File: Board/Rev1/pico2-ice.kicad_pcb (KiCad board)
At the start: 4 copper layers, 27.9 x 63.5 mm, 122 parts, among them J1 USB_C_Receptacle_USB2.0, J2 Conn_02x20_Odd_Even, J3 Conn_02x20_Odd_Even, J5 BM03B-SRSS-TB, J6 Conn_01x22_MountingPin, SW1 CS1213AGF260, SW2 CS1213AGF260, U1 NCP115AMX120TCG, U2 W25Q32JVSSIQ, U3 RP2350_80QFN, U4 TL431DBZ, U5 APS6404L-3SQN-SN, U6 ICE40UP5K-SG48ITR, U8 W25Q32JVSSIQ, U9 NCP115AMX330TCG, Y1 ABM8-272-T3

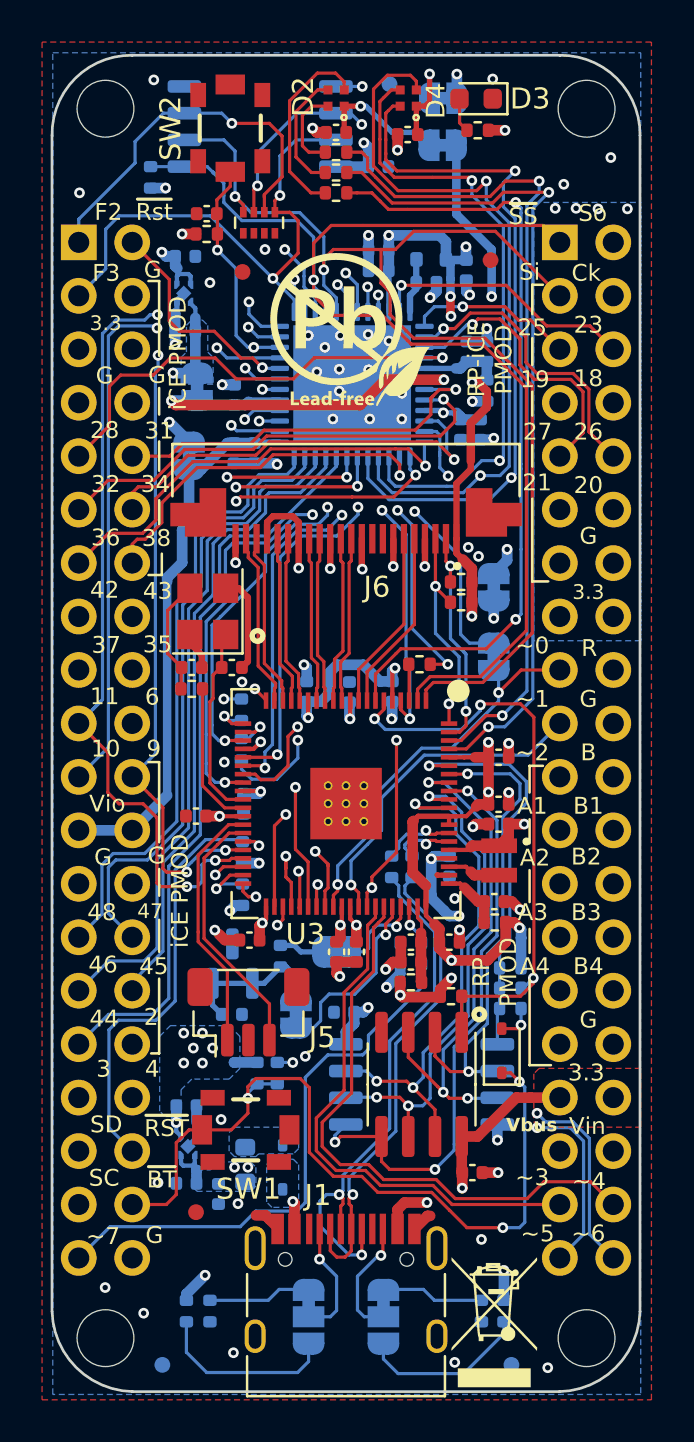
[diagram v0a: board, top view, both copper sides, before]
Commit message: Bugfixes for silkscreen PMOD, added DONE, unconnected RP22 pins, layout not yet complete
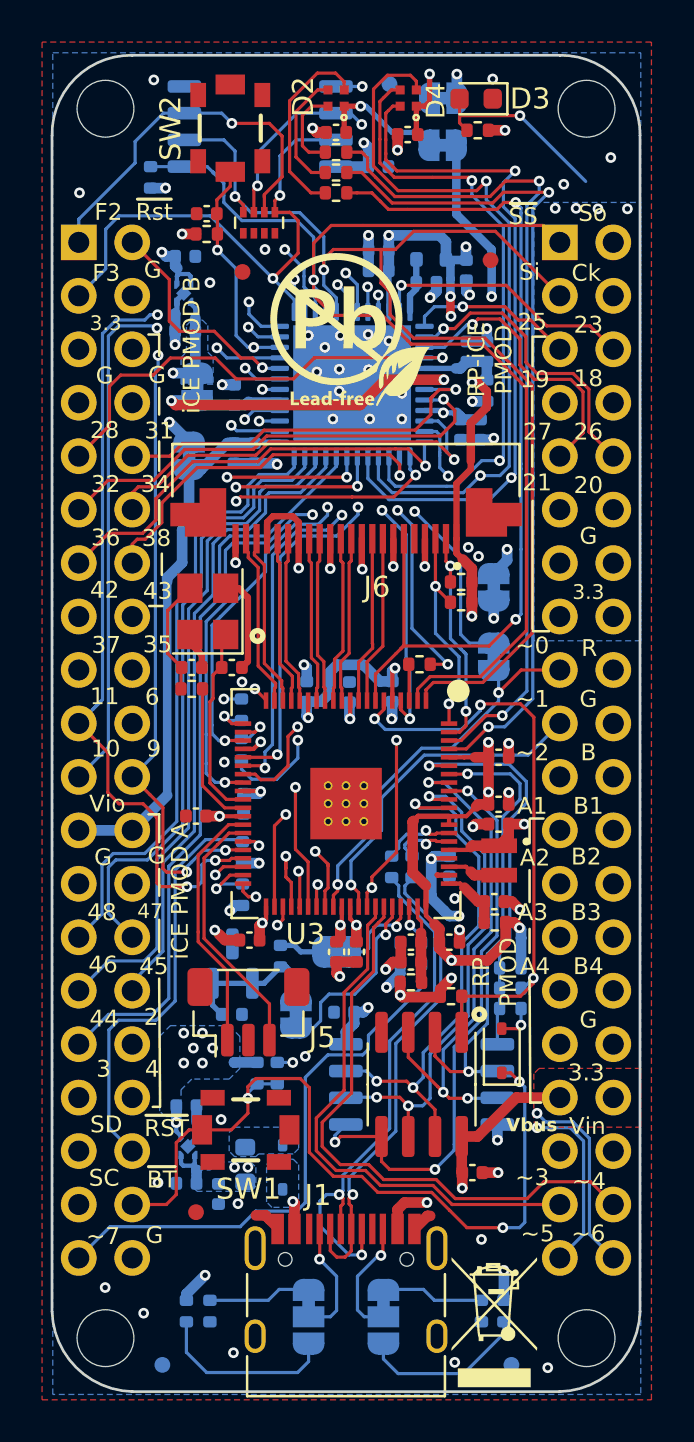
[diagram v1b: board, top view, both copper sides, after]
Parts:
- J6: value Conn_01x22_MountingPin -> FH12A-22S-0.5SH(55)
- R30, R31: value 0 -> SHORT
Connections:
- D3 pad 2: /ICE_DONE -> /ICE_DONE|ADC0
- J6 pad 5: /GPIO10 -> /LED_R
- J6 pad 6: /GPIO11 -> /LED_B
- J6 pad 8: unconnected-(J6-Pin_8-Pad8) -> /GPIO10
- J6 pad 9: unconnected-(J6-Pin_9-Pad9) -> /GPIO11
- R14 pad 1: /ICE_DONE -> /ICE_DONE|ADC0
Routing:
- net /ICE_DONE|ADC0: track 18.8 -> 27.7 mm, vias 2 -> 3
- net /LED_B: track 37.5 -> 42.8 mm
- net /ICE_DONE: track 1.65 -> 0.00 mm
- net /GPIO10: track 8.62 -> 8.00 mm
- net /GPIO11: track 8.58 -> 7.97 mm
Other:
- board text added: "iCE PMOD A"
- board text added: "iCE PMOD B"
- board text removed: "iCE PMOD"

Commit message: PCB file updated
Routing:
- net /ICE_DONE|ADC0: track 27.7 -> 51.9 mm
- net /LED_R: track 39.8 -> 50.1 mm, vias 2 -> 3
- net /ICE_27: track 37.0 -> 38.8 mm
- net /LED_B: track 42.8 -> 44.1 mm
- net +3V3: track 82.6 -> 83.4 mm

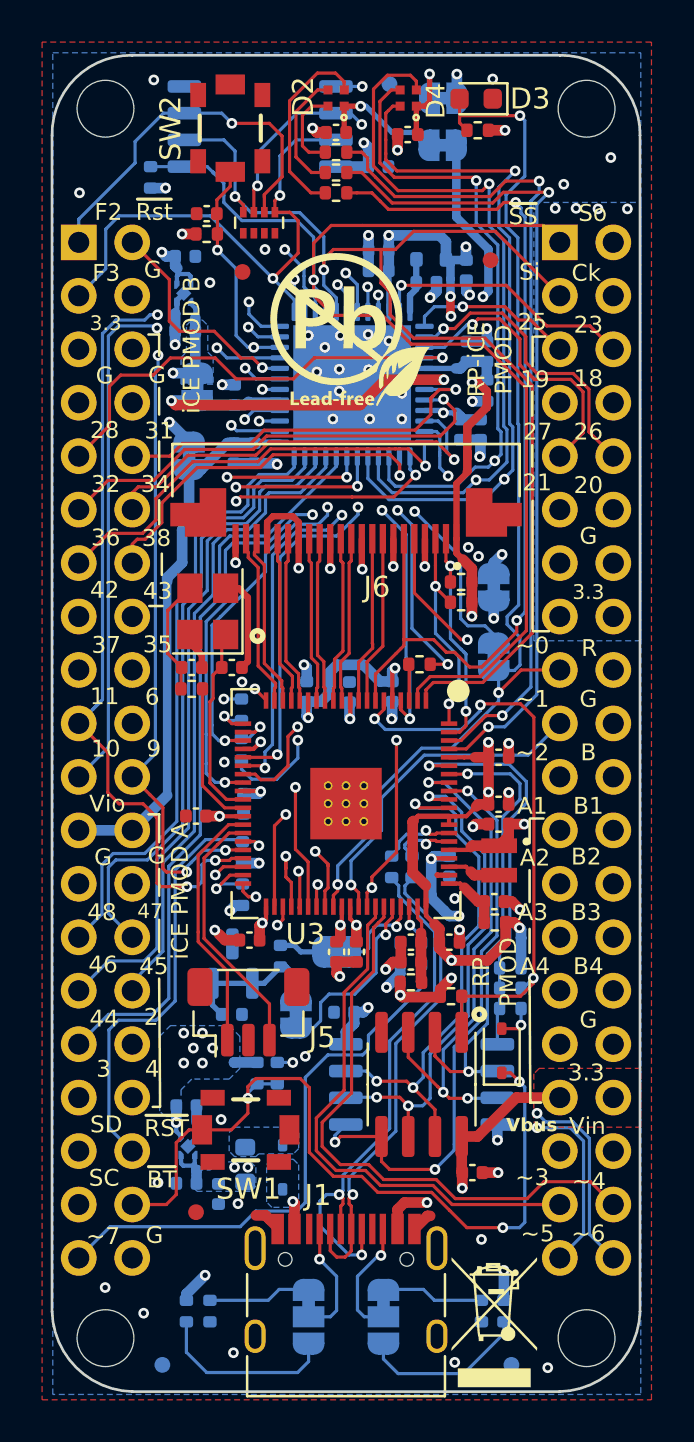
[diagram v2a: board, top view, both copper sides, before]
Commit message: Added voltage monitor
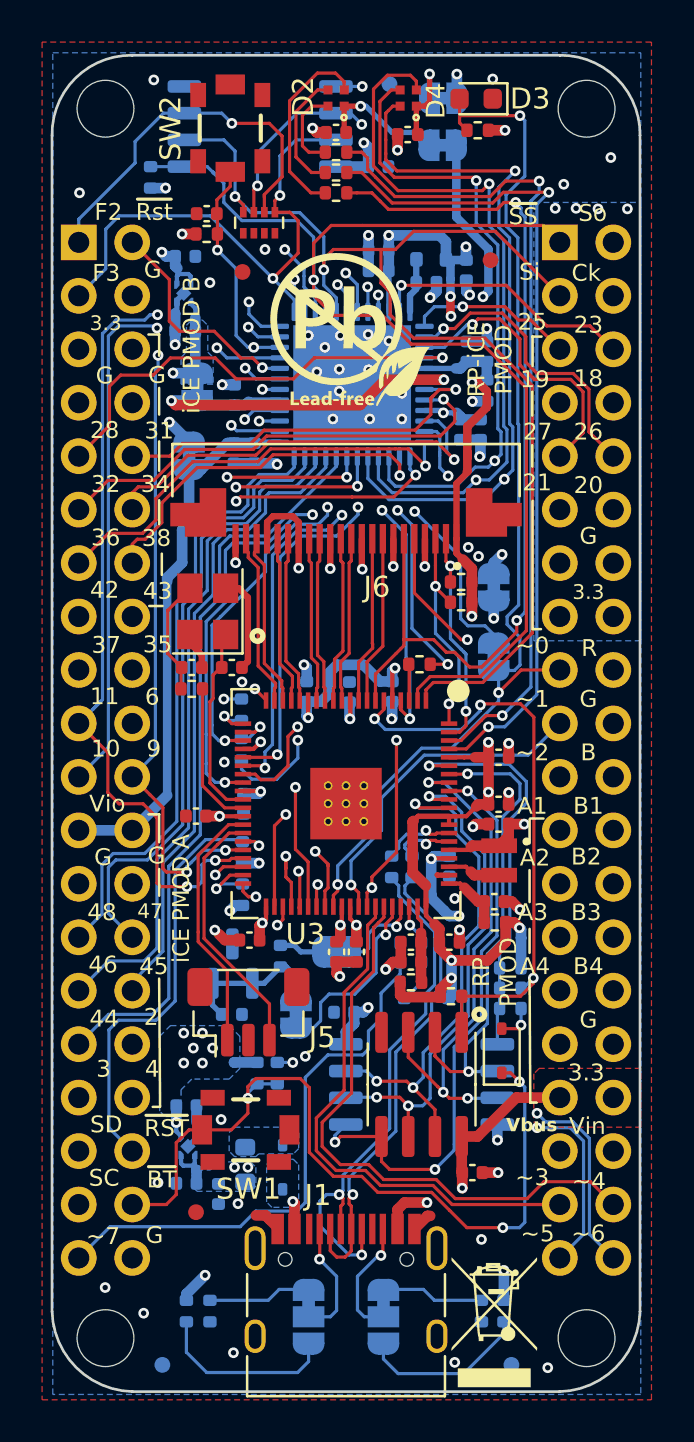
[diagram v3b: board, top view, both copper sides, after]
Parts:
- added D7: 1N5819WS, Diode_SMD:D_SOD-323, B.Cu at (76.2, 116.0)
- J6: value FH12A-22S-0.5SH(55) -> SFV22R-2STE1HLF
- R29: value 10K -> 2.2K
- moved R29 0.10 mm to (75.5, 114.2)
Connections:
- R28 pad 1: /ADC7 -> Net-(D7-A)
- R29 pad 1: V_{BUS} -> /ADC7
- R29 pad 2: /ADC7 -> Net-(D7-A)
- U3 pad 58: /ADC7 -> Net-(D7-A)
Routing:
- net V_{BUS}: track 20.9 -> 6.78 mm, vias 5 -> 4
- net Net-(D7-A): track 0.00 -> 5.00 mm, vias 0 -> 1
- net /ADC7: track 29.6 -> 26.1 mm, vias 1 -> 0
- net +3V3: track 83.4 -> 85.4 mm, vias 26 -> 25

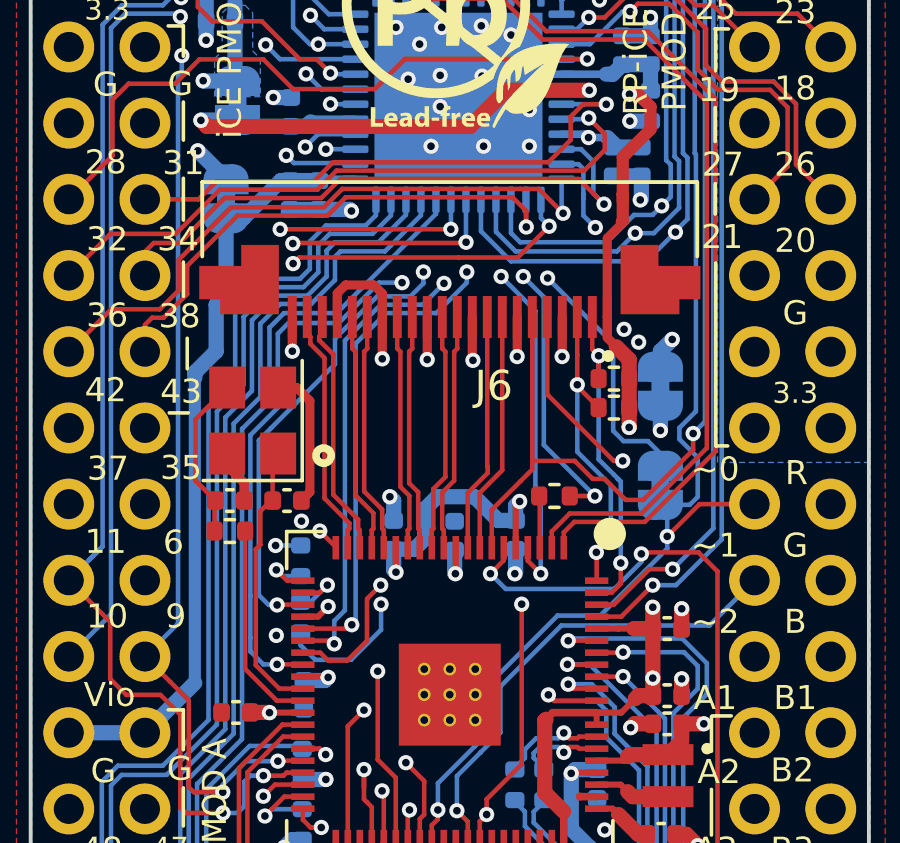
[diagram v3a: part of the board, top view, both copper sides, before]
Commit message: Unravelled the HSTX port after changing to a top contact part.
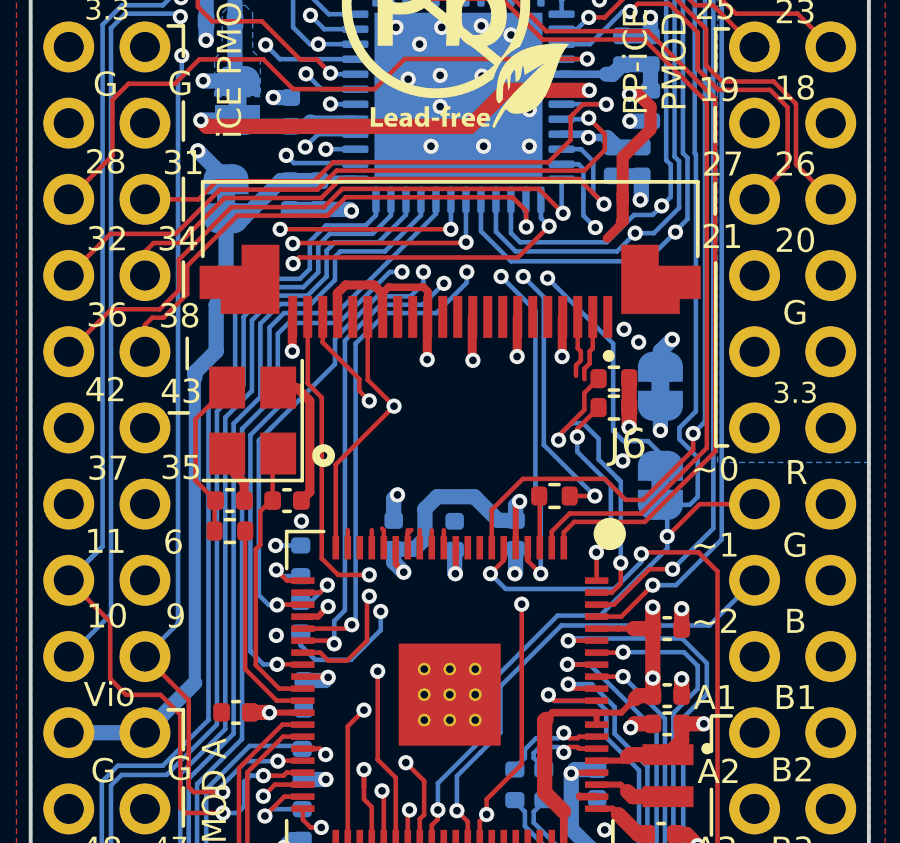
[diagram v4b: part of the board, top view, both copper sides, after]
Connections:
- J6 pad 1: +3V3 -> GND
- J6 pad 11: /Lane2_P -> /Lane0_P
- J6 pad 12: /Lane2_N -> /Lane0_N
- J6 pad 14: /Clock_P -> /GPIO10
- J6 pad 15: /Clock_N -> /GPIO11
- J6 pad 17: /Lane1_P -> /ICE_27
- J6 pad 18: /Lane1_N -> /ICE_19
- J6 pad 2: /SDA_GPIO2 -> /Lane2_P
- J6 pad 20: /Lane0_P -> /SCL_GPIO3
- J6 pad 21: /Lane0_N -> /SDA_GPIO2
- J6 pad 22: GND -> +3V3
- J6 pad 3: /SCL_GPIO3 -> /Lane2_N
- J6 pad 5: /LED_R -> /Clock_P
- J6 pad 6: /LED_B -> /Clock_N
- J6 pad 8: /GPIO10 -> /Lane1_P
- J6 pad 9: /GPIO11 -> /Lane1_N
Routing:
- net /SDA_GPIO2: track 47.0 -> 59.0 mm, vias 2 -> 3
- net /Lane0_P: track 8.29 -> 0.00 mm
- net /GPIO10: track 8.00 -> 0.00 mm
- net /GPIO11: track 7.97 -> 0.00 mm
- net /Lane0_N: track 8.29 -> 0.59 mm
- net /Lane1_N: track 8.00 -> 0.59 mm
- net /Lane1_P: track 8.00 -> 0.66 mm
- net /Clock_P: track 7.88 -> 0.59 mm
- net /Clock_N: track 7.88 -> 1.23 mm
- net /LED_R: track 50.1 -> 44.1 mm
- net /LED_B: track 44.1 -> 38.6 mm
- net /Lane2_N: track 7.92 -> 2.65 mm
- net /Lane2_P: track 7.92 -> 2.78 mm
- net +3V3: track 85.4 -> 81.7 mm, vias 25 -> 26
- net /ICE_27: track 38.8 -> 40.9 mm
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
